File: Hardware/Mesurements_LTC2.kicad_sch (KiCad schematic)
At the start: 12 parts, among them Q2 100V/2W, U2 BQ79614PAPRQ1

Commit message: Bms plug and play, 2nd iteration with the same pinout
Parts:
- U2: footprint footrpint:BQ79614PAPRQ1 -> Package_QFP:Texas_TQFP-64-1EP_10x10mm_P0.5mm_EP8x8mm_Mask4.44x4.44mm_ThermalVias

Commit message: nearly done
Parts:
- added C145: 0.47uF, Capacitor_SMD:C_0603_1608Metric_Pad1.08x0.95mm_HandSolder, symbol Device:C_Small
- added F45, F46: 400mA, Fuse:Fuse_0805_2012Metric, symbol Device:Fuse_Small
- added J11: Conn_01x02, Connector_Wire:SolderWire-0.127sqmm_1x02_P3.7mm_D0.48mm_OD1mm_Relief, symbol Connector_Generic:Conn_01x02
- added R15, R61: 300R, Resistor_SMD:R_0603_1608Metric, symbol Device:R_Small
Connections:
- net at U2.63 (BBN): now also R61.1
- net at U2.64 (BBP): now also R15.1
- new net: C145.1, F46.2, R61.2
- new net: C145.2, F45.2, R15.2
- new net: F45.1, J11.2 (Pin_2)
- new net: F46.1, J11.1 (Pin_1)
- no-connect marks 9 -> 7

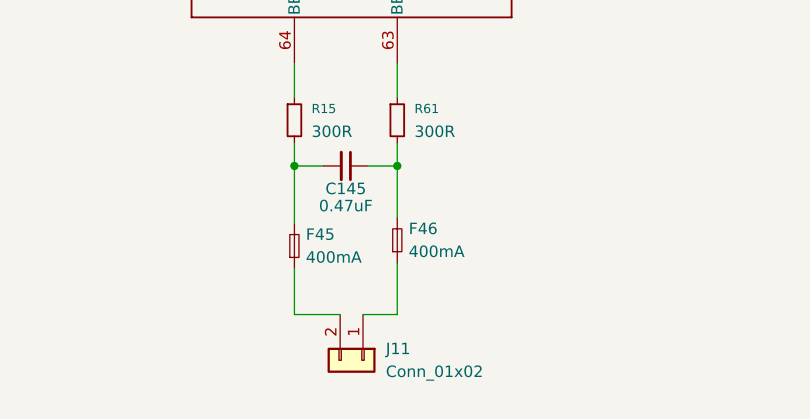
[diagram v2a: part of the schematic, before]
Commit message: New connectors jst_xh for low voltage side of bms
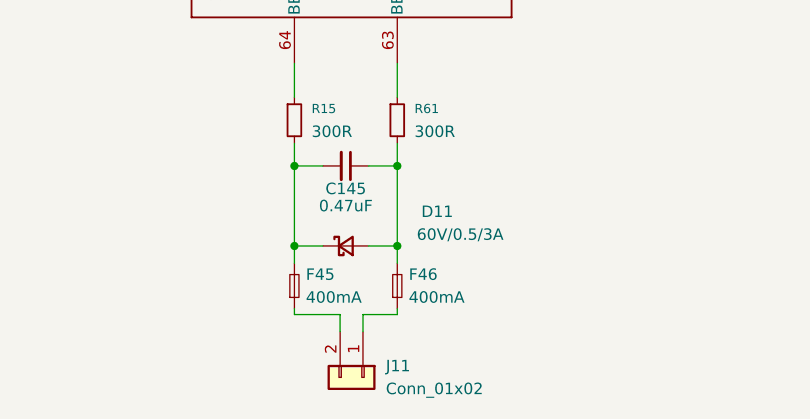
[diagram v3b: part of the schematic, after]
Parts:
- added D11: 60V/0.5/3A, Diode_SMD:D_SOD-123, symbol Device:D_Schottky_Small
- J11: footprint Connector_Wire:SolderWire-0.127sqmm_1x02_P3.7mm_D0.48mm_OD1mm_Relief -> Connector_JST:JST_XH_S2B-XH-A_1x02_P2.50mm_Horizontal
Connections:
- net at C145.1, F46.2, R61.2: now also D11.2 (A)
- net at C145.2, F45.2, R15.2: now also D11.1 (K)
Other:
- title: (none) -> Battery Management System for a high power gokart battery
- moved on the sheet: F45, F46

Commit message: No drc errors
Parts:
- removed C145: 0.47uF, Capacitor_SMD:C_0603_1608Metric_Pad1.08x0.95mm_HandSolder, symbol Device:C_Small
- removed D11: 60V/0.5/3A, Diode_SMD:D_SOD-123, symbol Device:D_Schottky_Small
- removed F45, F46: 400mA, Fuse:Fuse_0805_2012Metric, symbol Device:Fuse_Small
- removed J11: Conn_01x02, Connector_JST:JST_XH_S2B-XH-A_1x02_P2.50mm_Horizontal, symbol Connector_Generic:Conn_01x02
- removed R15, R61: 300R, Resistor_SMD:R_0603_1608Metric, symbol Device:R_Small
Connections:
- no-connect marks 7 -> 9
